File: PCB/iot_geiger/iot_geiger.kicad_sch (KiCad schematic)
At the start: 60 parts, among them J1 Program, J2 Display, J3 IO, J4 5V DC, J5 PM, Q1 BUK7M6R3, Q2 BC817, SW1 SW_Update, U1 NINA-W102, U2 AM2302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

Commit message: fix spiffs
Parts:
- added R19: 10K, Resistor_SMD:R_0603_1608Metric_Pad0.98x0.95mm_HandSolder, symbol Device:R
- V1: footprint (none) -> nina:Geiger
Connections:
- net GND: now also R19.1
- net at Q1.4 (G), R10.1: now also R19.2
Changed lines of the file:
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@@
   (junction (at 135.89 243.84) (diameter 0) (color 0 0 0 0)
   )
+  (junction (at 110.49 71.12) (diameter 0) (color 0 0 0 0)
+  )
   (junction (at 254 148.59) (diameter 0) (color 0 0 0 0)
   )
@@
     (stroke (width 0) (type default) (color 0 0 0 0))
   )
+  (wire (pts (xy 110.49 71.12) (xy 110.49 78.74))
+    (stroke (width 0) (type default) (color 0 0 0 0))
+  )
   (wire (pts (xy 186.69 74.93) (xy 186.69 78.74))
     (stroke (width 0) (type default) (color 0 0 0 0))
@@
     (stroke (width 0) (type default) (color 0 0 0 0))
   )
+  (wire (pts (xy 110.49 71.12) (xy 113.03 71.12))
+    (stroke (width 0) (type default) (color 0 0 0 0))
+  )
   (wire (pts (xy 248.92 173.99) (xy 261.62 173.99))
     (stroke (width 0) (type default) (color 0 0 0 0))
@@
     (stroke (width 0) (type default) (color 0 0 0 0))
   )
+  (wire (pts (xy 110.49 86.36) (xy 110.49 88.9))
+    (stroke (width 0) (type default) (color 0 0 0 0))
+  )
   (wire (pts (xy 135.89 256.54) (xy 147.32 256.54))
     (stroke (width 0) (type default) (color 0 0 0 0))
@@
     (stroke (width 0) (type default) (color 0 0 0 0))
   )
-  (wire (pts (xy 107.95 71.12) (xy 113.03 71.12))
+  (wire (pts (xy 107.95 71.12) (xy 110.49 71.12))
     (stroke (width 0) (type default) (color 0 0 0 0))
   )
@@
     )
     (pin "1")
+  )
+  (symbol (lib_id "Device:R") (at 110.49 82.55 180) (unit 1)
+    (in_bom yes) (on_board yes)
+    (property "Reference" "R19" (id 0) (at 113.03 83.82 90))
+    (property "Value" "10K" (id 1) (at 110.49 82.55 90))
+    (property "Footprint" "Resistor_SMD:R_0603_1608Metric_Pad0.98x0.95mm_HandSolder" (id 2) (at 112.268 82.55 90)
+      (effects (font (size 1.27 1.27)) hide)
+    )
+    (property "Datasheet" "~" (id 3) (at 110.49 82.55 0)
+      (effects (font (size 1.27 1.27)) hide)
+    )
+    (pin "1")
+    (pin "2")
   )
   (symbol (lib_id "Device:R") (at 320.04 191.77 90) (unit 1)
@@
     (pin "2")
   )
+  (symbol (lib_id "power:GND") (at 110.49 88.9 0) (unit 1)
+    (in_bom yes) (on_board yes) (fields_autoplaced)
+    (property "Reference" "#PWR0149" (id 0) (at 110.49 95.25 0)
+      (effects (font (size 1.27 1.27)) hide)
+    )
+    (property "Value" "GND" (id 1) (at 110.49 93.98 0))
+    (property "Footprint" "" (id 2) (at 110.49 88.9 0)
+      (effects (font (size 1.27 1.27)) hide)
+    )
+    (property "Datasheet" "" (id 3) (at 110.49 88.9 0)
+      (effects (font (size 1.27 1.27)) hide)
+    )
+    (pin "1")
+  )
   (symbol (lib_id "power:+5V") (at 83.82 241.3 0) (unit 1)
     (in_bom yes) (on_board yes)
@@
     (property "Reference" "V1" (id 0) (at 205.9964 67.31 90))
     (property "Value" "J305" (id 1) (at 205.9964 69.85 90))
-    (property "Footprint" "" (id 2) (at 204.47 69.85 0)
+    (property "Footprint" "nina:Geiger" (id 2) (at 204.47 69.85 0)
       (effects (font (size 1.27 1.27)) hide)
     )
@@
       (reference "#PWR0148") (unit 1) (value "+3.3V") (footprint "")
     )
+    (path "/c977af6e-9b25-4661-887b-74341ecf7991"
+      (reference "#PWR0149") (unit 1) (value "GND") (footprint "")
+    )
     (path "/7347f0c1-ce39-4191-a275-90b3efbc6d21"
       (reference "BZ1") (unit 1) (value "Buzzer") (footprint "Buzzer_Beeper:Buzzer_12x9.5RM7.6")
@@
       (reference "R18") (unit 1) (value "10K") (footprint "Resistor_SMD:R_0603_1608Metric_Pad0.98x0.95mm_HandSolder")
     )
+    (path "/08732a30-5b7f-491c-9f7e-c143a39ece72"
+      (reference "R19") (unit 1) (value "10K") (footprint "Resistor_SMD:R_0603_1608Metric_Pad0.98x0.95mm_HandSolder")
+    )
     (path "/b03b5b85-891a-4fa8-9e6b-aac2c5c95c0b"
       (reference "S1") (unit 1) (value "SYM_Flash_Small") (footprint "Symbol:Symbol_HighVoltage_Type2_CopperTop_VerySmall")
@@
     )
     (path "/e752b8a0-bf8a-496a-8250-e06335fc8fc0"
-      (reference "V1") (unit 1) (value "J305") (footprint "")
-    )
-  )
+      (reference "V1") (unit 1) (value "J305") (footprint "nina:Geiger")
+    )
+  )

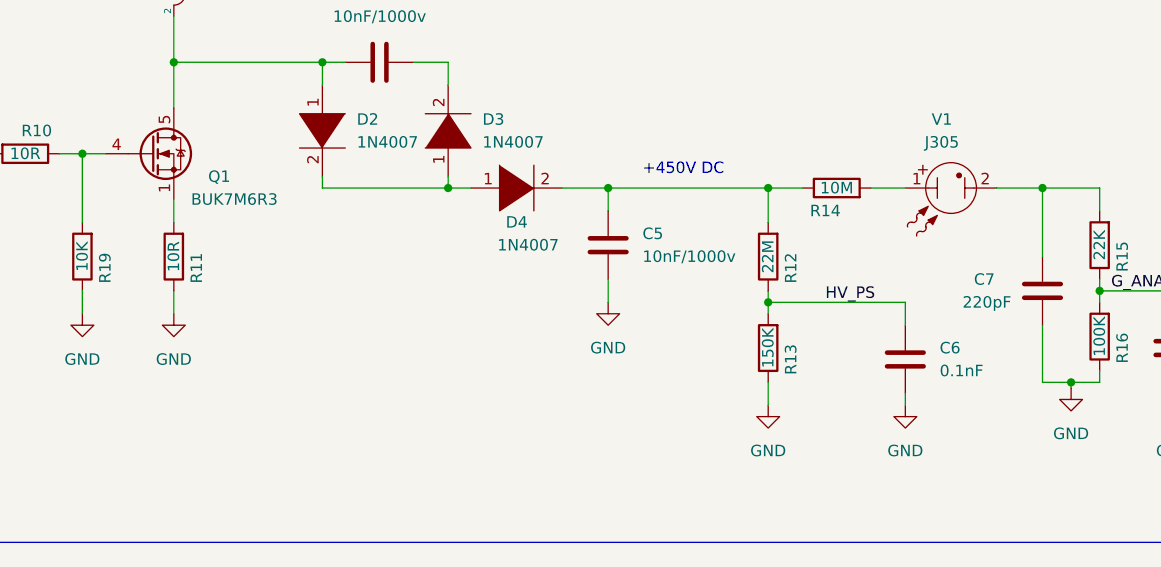
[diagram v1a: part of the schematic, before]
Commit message: Add PM sensor support
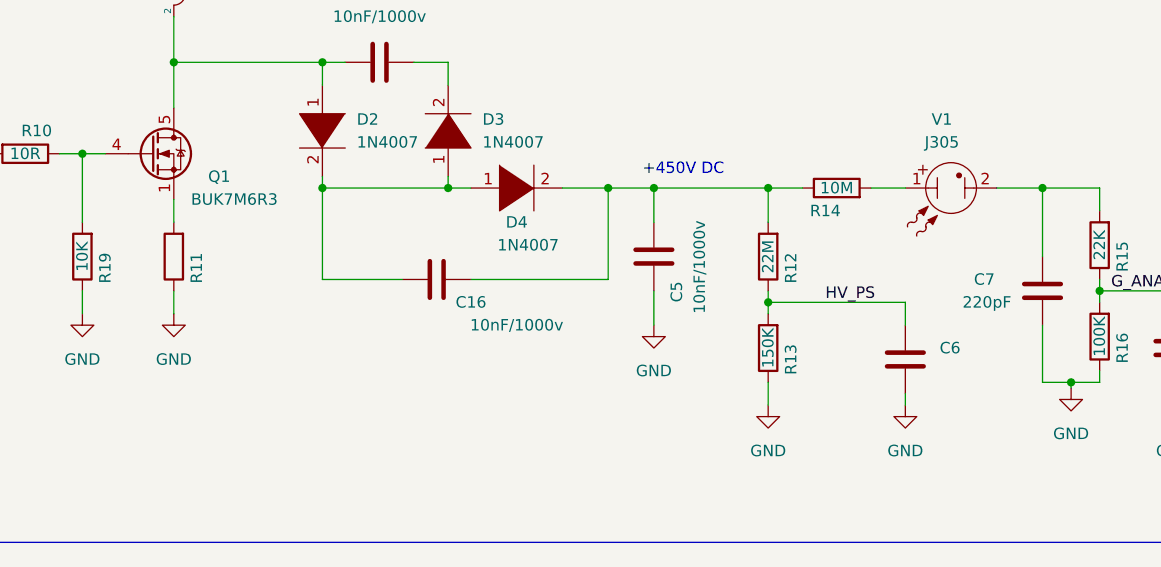
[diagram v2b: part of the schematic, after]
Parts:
- added C16: 10nF/1000v, Capacitor_THT:C_Disc_D7.5mm_W2.5mm_P5.00mm, symbol Device:C
- C6: value 0.1nF -> (none)
- R11: value 10R -> (none)
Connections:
- net at D2.2 (A), D3.1 (K), D4.1 (K): now also C16.1
- net at C5.2, D4.2 (A), R12.2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: now also C16.2
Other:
- moved on the sheet: C5
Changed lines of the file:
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@@
   (junction (at 129.54 156.21) (diameter 0) (color 0 0 0 0)
   )
+  (junction (at 137.16 74.93) (diameter 0) (color 0 0 0 0)
+  )
   (junction (at 186.69 74.93) (diameter 0) (color 0 0 0 0)
   )
@@
   (junction (at 168.91 74.93) (diameter 0) (color 0 0 0 0)
   )
+  (junction (at 173.99 74.93) (diameter 0) (color 0 0 0 0)
+  )
   (junction (at 151.13 74.93) (diameter 0) (color 0 0 0 0)
   )
@@
   (junction (at 120.65 60.96) (diameter 0) (color 0 0 0 0)
   )
+  (wire (pts (xy 173.99 74.93) (xy 186.69 74.93))
+    (stroke (width 0) (type default) (color 0 0 0 0))
+  )
   (wire (pts (xy 171.45 256.54) (xy 171.45 254))
     (stroke (width 0) (type default) (color 0 0 0 0))
@@
     (stroke (width 0) (type default) (color 0 0 0 0))
   )
+  (wire (pts (xy 173.99 86.36) (xy 173.99 90.17))
+    (stroke (width 0) (type default) (color 0 0 0 0))
+  )
   (wire (pts (xy 135.89 254) (xy 135.89 256.54))
     (stroke (width 0) (type default) (color 0 0 0 0))
@@
     (stroke (width 0) (type default) (color 0 0 0 0))
   )
-  (wire (pts (xy 168.91 85.09) (xy 168.91 87.63))
-    (stroke (width 0) (type default) (color 0 0 0 0))
-  )
   (wire (pts (xy 248.92 151.13) (xy 254 151.13))
     (stroke (width 0) (type default) (color 0 0 0 0))
@@
     (stroke (width 0) (type default) (color 0 0 0 0))
   )
+  (wire (pts (xy 137.16 74.93) (xy 137.16 85.09))
+    (stroke (width 0) (type default) (color 0 0 0 0))
+  )
   (wire (pts (xy 266.7 245.11) (xy 266.7 245.1741))
     (stroke (width 0) (type default) (color 0 0 0 0))
@@
     (stroke (width 0) (type default) (color 0 0 0 0))
   )
-  (wire (pts (xy 168.91 74.93) (xy 168.91 77.47))
-    (stroke (width 0) (type default) (color 0 0 0 0))
-  )
   (wire (pts (xy 217.17 74.93) (xy 223.52 74.93))
     (stroke (width 0) (type default) (color 0 0 0 0))
@@
     (stroke (width 0) (type default) (color 0 0 0 0))
   )
+  (wire (pts (xy 168.91 74.93) (xy 168.91 85.09))
+    (stroke (width 0) (type default) (color 0 0 0 0))
+  )
   (wire (pts (xy 255.27 77.47) (xy 255.27 80.01))
     (stroke (width 0) (type default) (color 0 0 0 0))
@@
     (stroke (width 0) (type default) (color 0 0 0 0))
   )
+  (wire (pts (xy 153.67 85.09) (xy 168.91 85.09))
+    (stroke (width 0) (type default) (color 0 0 0 0))
+  )
   (wire (pts (xy 212.09 74.93) (xy 217.17 74.93))
     (stroke (width 0) (type default) (color 0 0 0 0))
@@
     (stroke (width 0) (type default) (color 0 0 0 0))
   )
+  (wire (pts (xy 173.99 78.74) (xy 173.99 74.93))
+    (stroke (width 0) (type default) (color 0 0 0 0))
+  )
   (wire (pts (xy 327.66 90.17) (xy 327.66 99.06))
     (stroke (width 0) (type default) (color 0 0 0 0))
@@
     (stroke (width 0) (type default) (color 0 0 0 0))
   )
+  (wire (pts (xy 137.16 85.09) (xy 146.05 85.09))
+    (stroke (width 0) (type default) (color 0 0 0 0))
+  )
   (wire (pts (xy 186.69 86.36) (xy 186.69 87.63))
     (stroke (width 0) (type default) (color 0 0 0 0))
@@
     (stroke (width 0) (type default) (color 0 0 0 0))
   )
-  (wire (pts (xy 168.91 74.93) (xy 186.69 74.93))
+  (wire (pts (xy 168.91 74.93) (xy 173.99 74.93))
     (stroke (width 0) (type default) (color 0 0 0 0))
   )
@@
     )
     (pin "1")
+  )
+  (symbol (lib_id "Device:C") (at 149.86 85.09 90) (unit 1)
+    (in_bom yes) (on_board yes)
+    (property "Reference" "C16" (id 0) (at 153.67 87.63 90))
+    (property "Value" "10nF/1000v" (id 1) (at 158.75 90.17 90))
+    (property "Footprint" "Capacitor_THT:C_Disc_D7.5mm_W2.5mm_P5.00mm" (id 2) (at 153.67 84.1248 0)
+      (effects (font (size 1.27 1.27)) hide)
+    )
+    (property "Datasheet" "~" (id 3) (at 149.86 85.09 0)
+      (effects (font (size 1.27 1.27)) hide)
+    )
+    (pin "1")
+    (pin "2")
   )
   (symbol (lib_id "pspice:DIODE") (at 158.75 74.93 0) (unit 1)
@@
     (in_bom yes) (on_board yes)
     (property "Reference" "R11" (id 0) (at 123.19 83.82 90))
-    (property "Value" "10R" (id 1) (at 120.65 82.55 90))
+    (property "Value" "" (id 1) (at 120.65 82.55 90))
     (property "Footprint" "Resistor_SMD:R_0603_1608Metric_Pad0.98x0.95mm_HandSolder" (id 2) (at 122.428 82.55 90)
       (effects (font (size 1.27 1.27)) hide)
@@
     (pin "5")
   )
-  (symbol (lib_id "power:GND") (at 168.91 87.63 0) (unit 1)
-    (in_bom yes) (on_board yes) (fields_autoplaced)
-    (property "Reference" "#PWR0143" (id 0) (at 168.91 93.98 0)
-      (effects (font (size 1.27 1.27)) hide)
-    )
-    (property "Value" "GND" (id 1) (at 168.91 92.71 0))
-    (property "Footprint" "" (id 2) (at 168.91 87.63 0)
-      (effects (font (size 1.27 1.27)) hide)
-    )
-    (property "Datasheet" "" (id 3) (at 168.91 87.63 0)
+  (symbol (lib_id "power:GND") (at 173.99 90.17 0) (unit 1)
+    (in_bom yes) (on_board yes) (fields_autoplaced)
+    (property "Reference" "#PWR0143" (id 0) (at 173.99 96.52 0)
+      (effects (font (size 1.27 1.27)) hide)
+    )
+    (property "Value" "GND" (id 1) (at 173.99 95.25 0))
+    (property "Footprint" "" (id 2) (at 173.99 90.17 0)
+      (effects (font (size 1.27 1.27)) hide)
+    )
+    (property "Datasheet" "" (id 3) (at 173.99 90.17 0)
       (effects (font (size 1.27 1.27)) hide)
     )
@@
     (pin "2")
   )
-  (symbol (lib_id "Device:C") (at 168.91 81.28 180) (unit 1)
-    (in_bom yes) (on_board yes) (fields_autoplaced)
-    (property "Reference" "C5" (id 0) (at 172.72 80.0099 0)
+  (symbol (lib_id "Device:C") (at 173.99 82.55 180) (unit 1)
+    (in_bom yes) (on_board yes)
+    (property "Reference" "C5" (id 0) (at 176.53 87.63 90)
       (effects (font (size 1.27 1.27)) (justify right))
     )
-    (property "Value" "10nF/1000v" (id 1) (at 172.72 82.5499 0)
+    (property "Value" "10nF/1000v" (id 1) (at 179.07 88.9 90)
       (effects (font (size 1.27 1.27)) (justify right))
     )
-    (property "Footprint" "Capacitor_THT:C_Disc_D7.5mm_W2.5mm_P5.00mm" (id 2) (at 167.9448 77.47 0)
-      (effects (font (size 1.27 1.27)) hide)
-    )
-    (property "Datasheet" "~" (id 3) (at 168.91 81.28 0)
+    (property "Footprint" "Capacitor_THT:C_Disc_D7.5mm_W2.5mm_P5.00mm" (id 2) (at 173.0248 78.74 0)
+      (effects (font (size 1.27 1.27)) hide)
+    )
+    (property "Datasheet" "~" (id 3) (at 173.99 82.55 0)
       (effects (font (size 1.27 1.27)) hide)
     )
@@
       (effects (font (size 1.27 1.27)) (justify right))
     )
-    (property "Value" "0.1nF" (id 1) (at 205.74 95.2499 0)
+    (property "Value" "" (id 1) (at 205.74 95.2499 0)
       (effects (font (size 1.27 1.27)) (justify right))
     )
@@
     )
     (path "/c9562b20-4fc1-4825-a600-830338ae44b4"
-      (reference "C6") (unit 1) (value "0.1nF") (footprint "Capacitor_SMD:C_0603_1608Metric_Pad1.08x0.95mm_HandSolder")
+      (reference "C6") (unit 1) (value "100pF") (footprint "Capacitor_SMD:C_0603_1608Metric_Pad1.08x0.95mm_HandSolder")
     )
     (path "/195b7ec4-4d5b-48c4-a30d-b7836d007272"
@@
       (reference "C15") (unit 1) (value "100nF") (footprint "Capacitor_SMD:C_0603_1608Metric")
     )
+    (path "/2e710243-54dd-4d59-ae18-135e4df4f90e"
+      (reference "C16") (unit 1) (value "10nF/1000v") (footprint "Capacitor_THT:C_Disc_D7.5mm_W2.5mm_P5.00mm")
+    )
     (path "/77f7e2d9-ac97-463f-b1fa-ad2d7de64df4"
       (reference "D1") (unit 1) (value "Status") (footprint "LED_SMD:LED_0603_1608Metric_Pad1.05x0.95mm_HandSolder")
@@
     )
     (path "/39cc85b6-b2ae-43c4-b430-23a0e92f143e"
-      (reference "R11") (unit 1) (value "10R") (footprint "Resistor_SMD:R_0603_1608Metric_Pad0.98x0.95mm_HandSolder")
+      (reference "R11") (unit 1) (value "47R") (footprint "Resistor_SMD:R_0603_1608Metric_Pad0.98x0.95mm_HandSolder")
     )
     (path "/b0f99d33-b550-4722-8f78-fae8b3c3cd63"

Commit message: PCB updated
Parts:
- removed D2, D3, D4: 1N4007, Diode_THT:D_5W_P10.16mm_Horizontal, symbol pspice:DIODE
- removed Q1: BUK7M6R3, Package_TO_SOT_SMD:LFPAK33, symbol Transistor_FET:BUK7M6R3-40EX
- added D2, D3, D4: 1N4007, Diode_THT:D_DO-41_SOD81_P10.16mm_Horizontal, symbol Diode:1N4007
- added Q1: BSS123, Package_TO_SOT_SMD:SOT-23, symbol Transistor_FET:BSS123
- added R20: 22K, Resistor_SMD:R_0603_1608Metric_Pad0.98x0.95mm_HandSolder, symbol Device:R
- C3: value 100nF -> DNU
- C6: value (none) -> 100pF
- R11: value (none) -> 10R
- R12: value 22M -> 47M
- R13: value 150K -> 330K
- R15: value 22K -> 10K
- R16: value 100K -> 220K
- R3: value 10K* -> DNU
- R4: value 47K -> DNU
- R5: value 10K -> DNU
- R6, R8: value 47K -> 10K
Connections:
- net +3V3: now also R20.1
- net TEMP_SEN: now also R20.2
- net at R10.1, R19.2: now also Q1.1 (G)
- net at C16.1: now also D2.1 (K), D3.2 (A)
- net at C16.2, C5.2, R12.2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: now also D4.1 (K)
- net at R11.2: now also Q1.2 (S)
- net at C4.1, L1.2: now also D2.2 (A), Q1.3 (D)
- net at C4.2: now also D3.1 (K), D4.2 (A)
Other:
- moved on the sheet: C12, C16, C4, C5, C6, C7, Q2, R12, R13, R14, R15, R16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

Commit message: AP added
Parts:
- removed Q1: BSS123, Package_TO_SOT_SMD:SOT-23, symbol Transistor_FET:BSS123
- added Q1: PBHV8540Z, Package_TO_SOT_SMD:SOT-223, symbol Device:Q_NPN_BCEC
- R10: value 10R -> 2K2
- R11: value 10R -> 47R
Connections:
- net at R10.1, R19.2: now also Q1.1 (B)
- net at R11.2: now also Q1.3 (E)
- net at C4.1, D2.2 (A), L1.2: now also Q1.2 (C), Q1.4 (C)
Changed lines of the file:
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@@
   (junction (at 74.93 248.92) (diameter 0) (color 0 0 0 0)
   )
+  (junction (at 123.19 60.96) (diameter 0) (color 0 0 0 0)
+  )
   (junction (at 171.45 243.84) (diameter 0) (color 0 0 0 0)
   )
@@
     (stroke (width 0) (type default) (color 0 0 0 0))
   )
+  (wire (pts (xy 123.19 60.96) (xy 129.54 60.96))
+    (stroke (width 0) (type default) (color 0 0 0 0))
+  )
   (wire (pts (xy 154.94 243.84) (xy 161.29 243.84))
     (stroke (width 0) (type default) (color 0 0 0 0))
@@
     (stroke (width 0) (type default) (color 0 0 0 0))
   )
-  (wire (pts (xy 120.65 60.96) (xy 129.54 60.96))
+  (wire (pts (xy 120.65 60.96) (xy 123.19 60.96))
     (stroke (width 0) (type default) (color 0 0 0 0))
   )
@@
   )
   (wire (pts (xy 254 148.59) (xy 254 146.05))
+    (stroke (width 0) (type default) (color 0 0 0 0))
+  )
+  (wire (pts (xy 123.19 60.96) (xy 123.19 66.04))
     (stroke (width 0) (type default) (color 0 0 0 0))
   )
@@
     (in_bom yes) (on_board yes)
     (property "Reference" "R10" (id 0) (at 105.41 68.58 90))
-    (property "Value" "10R" (id 1) (at 104.14 71.12 90))
+    (property "Value" "2K2" (id 1) (at 104.14 71.12 90))
     (property "Footprint" "Resistor_SMD:R_0603_1608Metric_Pad0.98x0.95mm_HandSolder" (id 2) (at 104.14 69.342 90)
       (effects (font (size 1.27 1.27)) hide)
@@
     (in_bom yes) (on_board yes)
     (property "Reference" "R11" (id 0) (at 123.19 83.82 90))
-    (property "Value" "10R" (id 1) (at 120.65 82.55 90))
+    (property "Value" "47R" (id 1) (at 120.65 82.55 90))
     (property "Footprint" "Resistor_SMD:R_0603_1608Metric_Pad0.98x0.95mm_HandSolder" (id 2) (at 122.428 82.55 90)
       (effects (font (size 1.27 1.27)) hide)
@@
     (pin "1")
   )
+  (symbol (lib_id "Device:Q_NPN_BCEC") (at 118.11 71.12 0) (unit 1)
+    (in_bom yes) (on_board yes) (fields_autoplaced)
+    (property "Reference" "Q1" (id 0) (at 124.46 69.8499 0)
+      (effects (font (size 1.27 1.27)) (justify left))
+    )
+    (property "Value" "PBHV8540Z" (id 1) (at 124.46 72.3899 0)
+      (effects (font (size 1.27 1.27)) (justify left))
+    )
+    (property "Footprint" "Package_TO_SOT_SMD:SOT-223" (id 2) (at 123.19 68.58 0)
+      (effects (font (size 1.27 1.27)) hide)
+    )
+    (property "Datasheet" "~" (id 3) (at 118.11 71.12 0)
+      (effects (font (size 1.27 1.27)) hide)
+    )
+    (pin "1")
+    (pin "2")
+    (pin "3")
+    (pin "4")
+  )
   (symbol (lib_id "power:+5V") (at 135.89 242.57 0) (unit 1)
     (in_bom yes) (on_board yes)
@@
     )
     (pin "1")
-  )
-  (symbol (lib_id "Transistor_FET:BSS123") (at 118.11 71.12 0) (unit 1)
-    (in_bom yes) (on_board yes) (fields_autoplaced)
-    (property "Reference" "Q1" (id 0) (at 124.46 69.8499 0)
-      (effects (font (size 1.27 1.27)) (justify left))
-    )
-    (property "Value" "BSS123" (id 1) (at 124.46 72.3899 0)
-      (effects (font (size 1.27 1.27)) (justify left))
-    )
-    (property "Footprint" "Package_TO_SOT_SMD:SOT-23" (id 2) (at 123.19 73.025 0)
-      (effects (font (size 1.27 1.27) italic) (justify left) hide)
-    )
-    (property "Datasheet" "http://www.diodes.com/assets/Datasheets/ds30366.pdf" (id 3) (at 118.11 71.12 0)
-      (effects (font (size 1.27 1.27)) (justify left) hide)
-    )
-    (pin "1")
-    (pin "2")
-    (pin "3")
   )
   (symbol (lib_id "Connector:Barrel_Jack_Switch") (at 64.77 246.38 0) (unit 1)
@@
       (reference "L1") (unit 1) (value "10mH") (footprint "Inductor_SMD:L_12x12mm_H6mm")
     )
-    (path "/81671305-2324-43b4-8e1a-dfab6325e3d6"
-      (reference "Q1") (unit 1) (value "BSS123") (footprint "Package_TO_SOT_SMD:SOT-23")
+    (path "/6d3fe2e2-f863-41e5-8e0c-e75fee38bb03"
+      (reference "Q1") (unit 1) (value "PBHV8540Z") (footprint "Package_TO_SOT_SMD:SOT-223")
     )
     (path "/3ce191a3-9985-4bc7-98f2-9cbe9be43819"
@@
     )
     (path "/3988b4dd-bf53-42b2-bcb8-0a45afa97f57"
-      (reference "R10") (unit 1) (value "10R") (footprint "Resistor_SMD:R_0603_1608Metric_Pad0.98x0.95mm_HandSolder")
+      (reference "R10") (unit 1) (value "2K2") (footprint "Resistor_SMD:R_0603_1608Metric_Pad0.98x0.95mm_HandSolder")
     )
     (path "/39cc85b6-b2ae-43c4-b430-23a0e92f143e"
-      (reference "R11") (unit 1) (value "10R") (footprint "Resistor_SMD:R_0603_1608Metric_Pad0.98x0.95mm_HandSolder")
+      (reference "R11") (unit 1) (value "47R") (footprint "Resistor_SMD:R_0603_1608Metric_Pad0.98x0.95mm_HandSolder")
     )
     (path "/b0f99d33-b550-4722-8f78-fae8b3c3cd63"
